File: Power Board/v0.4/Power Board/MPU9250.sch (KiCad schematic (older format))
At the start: 4 parts, among them U4 MPU-9250

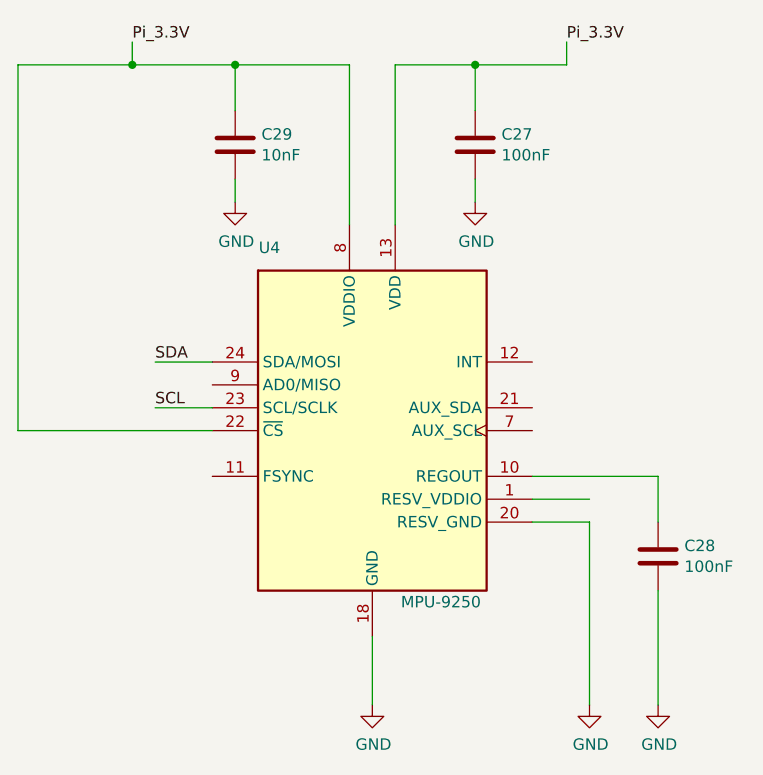
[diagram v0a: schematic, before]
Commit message: Updated board dimensions and mt. holes, tweaked MPU schematic.
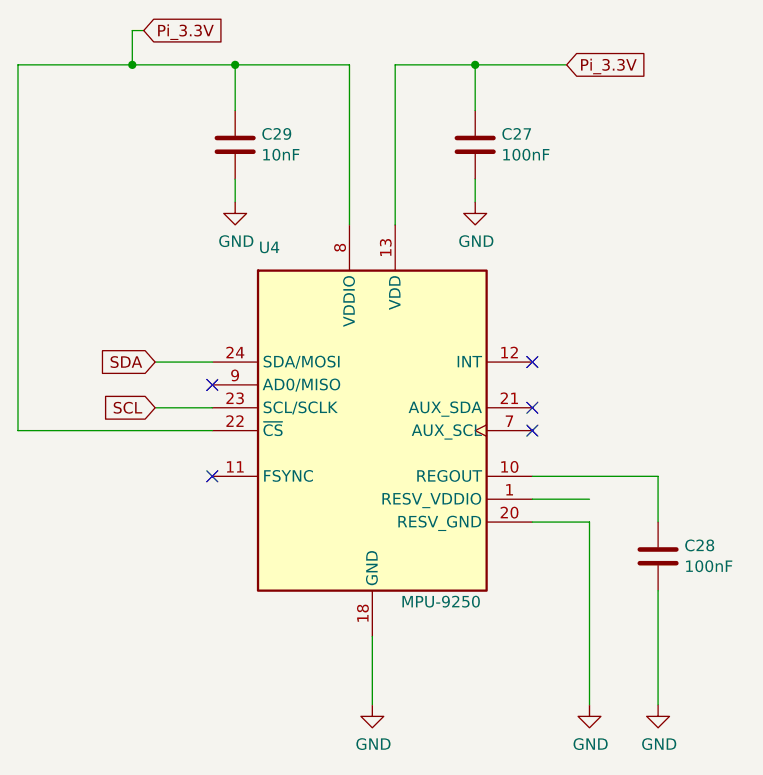
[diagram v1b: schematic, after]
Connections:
- no-connect marks 0 -> 5
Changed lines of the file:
@@
 	4550 4400 4550 4700
 $Comp
-L power:GND #PWR?
+L power:GND #PWR0111
 U 1 1 5CBBE5DC
 P 5500 4700
-F 0 "#PWR?" H 5500 4450 50  0001 C CNN
+F 0 "#PWR0111" H 5500 4450 50  0001 C CNN
 F 1 "GND" H 5505 4527 50  0000 C CNN
 F 2 "" H 5500 4700 50  0001 C CNN
@@
 $EndComp
 $Comp
-L power:GND #PWR?
+L power:GND #PWR0112
 U 1 1 5CBBE6B4
 P 4550 4700
-F 0 "#PWR?" H 4550 4450 50  0001 C CNN
+F 0 "#PWR0112" H 4550 4450 50  0001 C CNN
 F 1 "GND" H 4555 4527 50  0000 C CNN
 F 2 "" H 4550 4700 50  0001 C CNN
@@
 Wire Wire Line
 	5250 3800 5500 3800
-Text Label 3600 3200 0    50   ~ 0
-SDA
-Text Label 3600 3400 0    50   ~ 0
-SCL
 Wire Wire Line
 	3850 3200 3600 3200
@@
 	5800 4200 5800 4700
 $Comp
-L power:GND #PWR?
+L power:GND #PWR0113
 U 1 1 5CBC7883
 P 5800 4700
-F 0 "#PWR?" H 5800 4450 50  0001 C CNN
+F 0 "#PWR0113" H 5800 4450 50  0001 C CNN
 F 1 "GND" H 5805 4527 50  0000 C CNN
 F 2 "" H 5800 4700 50  0001 C CNN
@@
 $EndComp
 $Comp
-L power:GND #PWR?
+L power:GND #PWR0114
 U 1 1 5CBC907B
 P 5000 2500
-F 0 "#PWR?" H 5000 2250 50  0001 C CNN
+F 0 "#PWR0114" H 5000 2250 50  0001 C CNN
 F 1 "GND" H 5005 2327 50  0000 C CNN
 F 2 "" H 5000 2500 50  0001 C CNN
@@
 	4450 1900 3950 1900
 Wire Wire Line
-	3500 1900 3500 1800
-Wire Wire Line
 	4450 1900 4450 2600
 Wire Wire Line
@@
 	4650 1900 5000 1900
 Wire Wire Line
-	5400 1900 5400 1800
-Wire Wire Line
 	4650 1900 4650 2600
 Wire Wire Line
@@
 	5000 1900 5400 1900
 $Comp
-L power:GND #PWR?
+L power:GND #PWR0115
 U 1 1 5CBCC161
 P 3950 2500
-F 0 "#PWR?" H 3950 2250 50  0001 C CNN
+F 0 "#PWR0115" H 3950 2250 50  0001 C CNN
 F 1 "GND" H 3955 2327 50  0000 C CNN
 F 2 "" H 3950 2500 50  0001 C CNN
@@
 	3000 1900 3000 3500
 Connection ~ 3500 1900
-Text Label 3500 1800 0    50   ~ 0
+Text GLabel 5400 1900 2    50   Input ~ 0
 Pi_3.3V
-Text Label 5400 1800 0    50   ~ 0
+NoConn ~ 5250 3200
+NoConn ~ 5250 3400
+NoConn ~ 5250 3500
+NoConn ~ 3850 3700
+NoConn ~ 3850 3300
+Text GLabel 3600 3200 0    50   Input ~ 0
+SDA
+Text GLabel 3600 3400 0    50   Input ~ 0
+SCL
+Text GLabel 3550 1750 2    50   Input ~ 0
 Pi_3.3V
+Wire Wire Line
+	3500 1750 3550 1750
+Wire Wire Line
+	3500 1750 3500 1900
 $EndSCHEMATC

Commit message: Revert "Updated board dimensions and mt. holes, tweaked MPU schematic."
This reverts commit 6936a160ef8a0f8efd2e8f2d18775030a6ae8800.
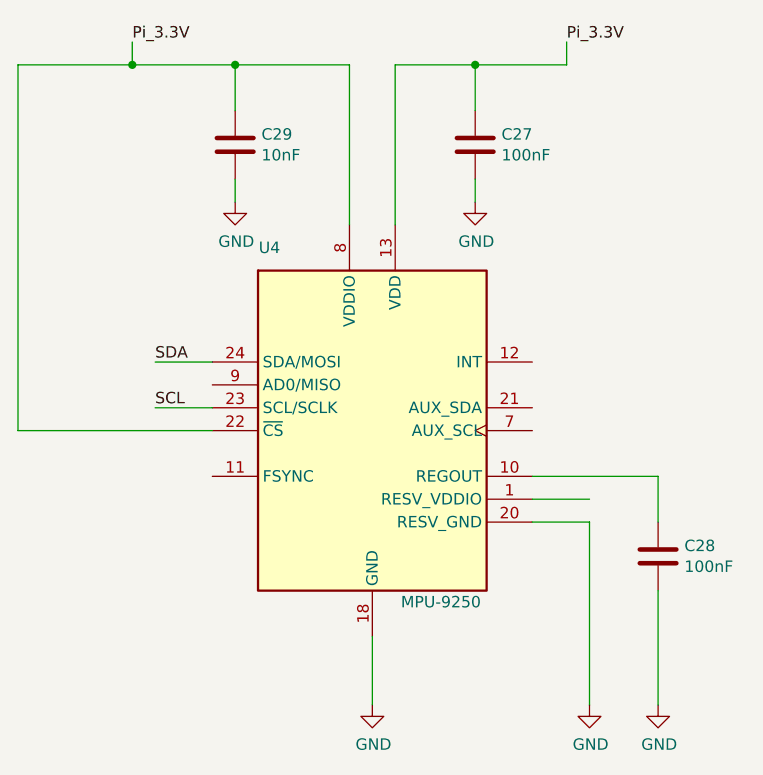
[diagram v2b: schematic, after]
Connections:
- no-connect marks 5 -> 0
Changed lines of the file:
@@
 	4550 4400 4550 4700
 $Comp
-L power:GND #PWR0111
+L power:GND #PWR?
 U 1 1 5CBBE5DC
 P 5500 4700
-F 0 "#PWR0111" H 5500 4450 50  0001 C CNN
+F 0 "#PWR?" H 5500 4450 50  0001 C CNN
 F 1 "GND" H 5505 4527 50  0000 C CNN
 F 2 "" H 5500 4700 50  0001 C CNN
@@
 $EndComp
 $Comp
-L power:GND #PWR0112
+L power:GND #PWR?
 U 1 1 5CBBE6B4
 P 4550 4700
-F 0 "#PWR0112" H 4550 4450 50  0001 C CNN
+F 0 "#PWR?" H 4550 4450 50  0001 C CNN
 F 1 "GND" H 4555 4527 50  0000 C CNN
 F 2 "" H 4550 4700 50  0001 C CNN
@@
 Wire Wire Line
 	5250 3800 5500 3800
+Text Label 3600 3200 0    50   ~ 0
+SDA
+Text Label 3600 3400 0    50   ~ 0
+SCL
 Wire Wire Line
 	3850 3200 3600 3200
@@
 	5800 4200 5800 4700
 $Comp
-L power:GND #PWR0113
+L power:GND #PWR?
 U 1 1 5CBC7883
 P 5800 4700
-F 0 "#PWR0113" H 5800 4450 50  0001 C CNN
+F 0 "#PWR?" H 5800 4450 50  0001 C CNN
 F 1 "GND" H 5805 4527 50  0000 C CNN
 F 2 "" H 5800 4700 50  0001 C CNN
@@
 $EndComp
 $Comp
-L power:GND #PWR0114
+L power:GND #PWR?
 U 1 1 5CBC907B
 P 5000 2500
-F 0 "#PWR0114" H 5000 2250 50  0001 C CNN
+F 0 "#PWR?" H 5000 2250 50  0001 C CNN
 F 1 "GND" H 5005 2327 50  0000 C CNN
 F 2 "" H 5000 2500 50  0001 C CNN
@@
 	4450 1900 3950 1900
 Wire Wire Line
+	3500 1900 3500 1800
+Wire Wire Line
 	4450 1900 4450 2600
 Wire Wire Line
@@
 	4650 1900 5000 1900
 Wire Wire Line
+	5400 1900 5400 1800
+Wire Wire Line
 	4650 1900 4650 2600
 Wire Wire Line
@@
 	5000 1900 5400 1900
 $Comp
-L power:GND #PWR0115
+L power:GND #PWR?
 U 1 1 5CBCC161
 P 3950 2500
-F 0 "#PWR0115" H 3950 2250 50  0001 C CNN
+F 0 "#PWR?" H 3950 2250 50  0001 C CNN
 F 1 "GND" H 3955 2327 50  0000 C CNN
 F 2 "" H 3950 2500 50  0001 C CNN
@@
 	3000 1900 3000 3500
 Connection ~ 3500 1900
-Text GLabel 5400 1900 2    50   Input ~ 0
+Text Label 3500 1800 0    50   ~ 0
 Pi_3.3V
-NoConn ~ 5250 3200
-NoConn ~ 5250 3400
-NoConn ~ 5250 3500
-NoConn ~ 3850 3700
-NoConn ~ 3850 3300
-Text GLabel 3600 3200 0    50   Input ~ 0
-SDA
-Text GLabel 3600 3400 0    50   Input ~ 0
-SCL
-Text GLabel 3550 1750 2    50   Input ~ 0
+Text Label 5400 1800 0    50   ~ 0
 Pi_3.3V
-Wire Wire Line
-	3500 1750 3550 1750
-Wire Wire Line
-	3500 1750 3500 1900
 $EndSCHEMATC

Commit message: Widen board to 70mm, delineate mechanical keepout zones.
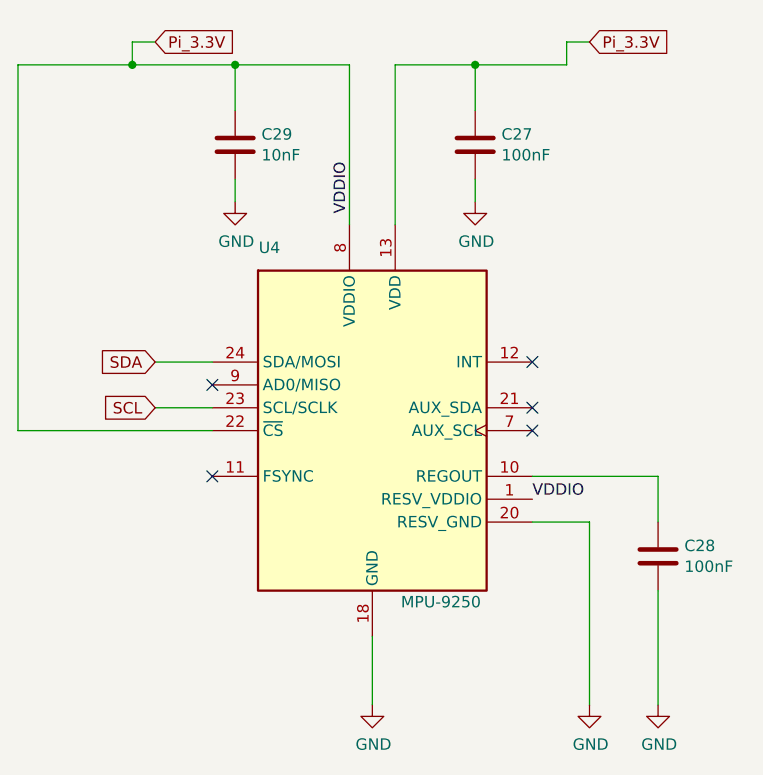
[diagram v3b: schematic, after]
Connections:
- net labels added: VDDIO
- wire segments 24 -> 25
- no-connect marks 0 -> 5
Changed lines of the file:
@@
 	4550 4400 4550 4700
 $Comp
-L power:GND #PWR?
+L power:GND #PWR0111
 U 1 1 5CBBE5DC
 P 5500 4700
-F 0 "#PWR?" H 5500 4450 50  0001 C CNN
+F 0 "#PWR0111" H 5500 4450 50  0001 C CNN
 F 1 "GND" H 5505 4527 50  0000 C CNN
 F 2 "" H 5500 4700 50  0001 C CNN
@@
 $EndComp
 $Comp
-L power:GND #PWR?
+L power:GND #PWR0112
 U 1 1 5CBBE6B4
 P 4550 4700
-F 0 "#PWR?" H 4550 4450 50  0001 C CNN
+F 0 "#PWR0112" H 4550 4450 50  0001 C CNN
 F 1 "GND" H 4555 4527 50  0000 C CNN
 F 2 "" H 4550 4700 50  0001 C CNN
@@
 Wire Wire Line
 	3850 3500 3000 3500
-Wire Wire Line
-	5250 3800 5500 3800
-Text Label 3600 3200 0    50   ~ 0
-SDA
-Text Label 3600 3400 0    50   ~ 0
-SCL
 Wire Wire Line
 	3850 3200 3600 3200
@@
 	5800 4200 5800 4700
 $Comp
-L power:GND #PWR?
+L power:GND #PWR0113
 U 1 1 5CBC7883
 P 5800 4700
-F 0 "#PWR?" H 5800 4450 50  0001 C CNN
+F 0 "#PWR0113" H 5800 4450 50  0001 C CNN
 F 1 "GND" H 5805 4527 50  0000 C CNN
 F 2 "" H 5800 4700 50  0001 C CNN
@@
 $EndComp
 $Comp
-L power:GND #PWR?
+L power:GND #PWR0114
 U 1 1 5CBC907B
 P 5000 2500
-F 0 "#PWR?" H 5000 2250 50  0001 C CNN
+F 0 "#PWR0114" H 5000 2250 50  0001 C CNN
 F 1 "GND" H 5005 2327 50  0000 C CNN
 F 2 "" H 5000 2500 50  0001 C CNN
@@
 	5000 1900 5400 1900
 $Comp
-L power:GND #PWR?
+L power:GND #PWR0115
 U 1 1 5CBCC161
 P 3950 2500
-F 0 "#PWR?" H 3950 2250 50  0001 C CNN
+F 0 "#PWR0115" H 3950 2250 50  0001 C CNN
 F 1 "GND" H 3955 2327 50  0000 C CNN
 F 2 "" H 3950 2500 50  0001 C CNN
@@
 	3000 1900 3000 3500
 Connection ~ 3500 1900
-Text Label 3500 1800 0    50   ~ 0
+Text GLabel 5500 1800 2    50   Input ~ 0
 Pi_3.3V
-Text Label 5400 1800 0    50   ~ 0
+Text GLabel 3600 1800 2    50   Input ~ 0
 Pi_3.3V
+Wire Wire Line
+	3500 1800 3600 1800
+Wire Wire Line
+	5500 1800 5400 1800
+Text GLabel 3600 3200 0    50   Input ~ 0
+SDA
+Text GLabel 3600 3400 0    50   Input ~ 0
+SCL
+NoConn ~ 5250 3200
+NoConn ~ 5250 3400
+NoConn ~ 5250 3500
+NoConn ~ 3850 3700
+NoConn ~ 3850 3300
+Text Label 5250 3800 0    50   ~ 0
+VDDIO
+Text Label 4450 2550 1    50   ~ 0
+VDDIO
 $EndSCHEMATC

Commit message: Update BOM.  Change R20 to 0603 package.
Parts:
- C27, C28: Digikey No. (none) -> -; Manufacturer (none) -> Murata; Part No. (none) -> GRM188R71C104KA01D
- C29: Digikey No. (none) -> -; Manufacturer (none) -> Murata; Part No. (none) -> GRM188R71H103KA01D
- U4: Digikey No. (none) -> 1428-1019-1-ND; Manufacturer (none) -> InvenSense; Part No. (none) -> MPU-9250
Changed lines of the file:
@@
 F 2 "Capacitor_SMD:C_0603_1608Metric" H 5838 3900 50  0001 C CNN
 F 3 "~" H 5800 4050 50  0001 C CNN
+F 4 "-" H 0   0   50  0001 C CNN "Digikey No."
+F 5 "Murata" H 0   0   50  0001 C CNN "Manufacturer"
+F 6 "GRM188R71C104KA01D" H 0   0   50  0001 C CNN "Part No."
 	1    5800 4050
 	1    0    0    -1
@@
 F 2 "Capacitor_SMD:C_0603_1608Metric" H 3988 2100 50  0001 C CNN
 F 3 "~" H 3950 2250 50  0001 C CNN
+F 4 "-" H 0   0   50  0001 C CNN "Digikey No."
+F 5 "Murata" H 0   0   50  0001 C CNN "Manufacturer"
+F 6 "GRM188R71H103KA01D" H 0   0   50  0001 C CNN "Part No."
 	1    3950 2250
 	1    0    0    -1
@@
 F 2 "Capacitor_SMD:C_0603_1608Metric" H 5115 2159 50  0001 L CNN
 F 3 "~" H 5000 2250 50  0001 C CNN
+F 4 "-" H 0   0   50  0001 C CNN "Digikey No."
+F 5 "Murata" H 0   0   50  0001 C CNN "Manufacturer"
+F 6 "GRM188R71C104KA01D" H 0   0   50  0001 C CNN "Part No."
 	1    5000 2250
 	1    0    0    -1
@@
 F 2 "Sensor_Motion:InvenSense_QFN-24_3x3mm_P0.4mm" H 4550 2500 50  0001 C CNN
 F 3 "https://store.invensense.com/datasheets/invensense/MPU9250REV1.0.pdf" H 4550 3350 50  0001 C CNN
+F 4 "1428-1019-1-ND" H 0   0   50  0001 C CNN "Digikey No."
+F 5 "InvenSense" H 0   0   50  0001 C CNN "Manufacturer"
+F 6 "MPU-9250" H 0   0   50  0001 C CNN "Part No."
 	1    4550 3500
 	1    0    0    -1
